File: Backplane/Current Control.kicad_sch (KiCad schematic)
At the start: 28 parts, among them Q25 TPHR8504PL,LQ(M1W, Q26 TPHR8504PL,LQ(M1W, U28 LM393, U29 UCC27324DR, U3 LM358, U32 MCP4725A0T-E/CH, U33 MCP4725A0T-E/CH

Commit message: Done with layout for first current control
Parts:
- U3: footprint (none) -> COMPONENTS:SOP-8_L4.9-W3.9-P1.27-LS6.0-BL

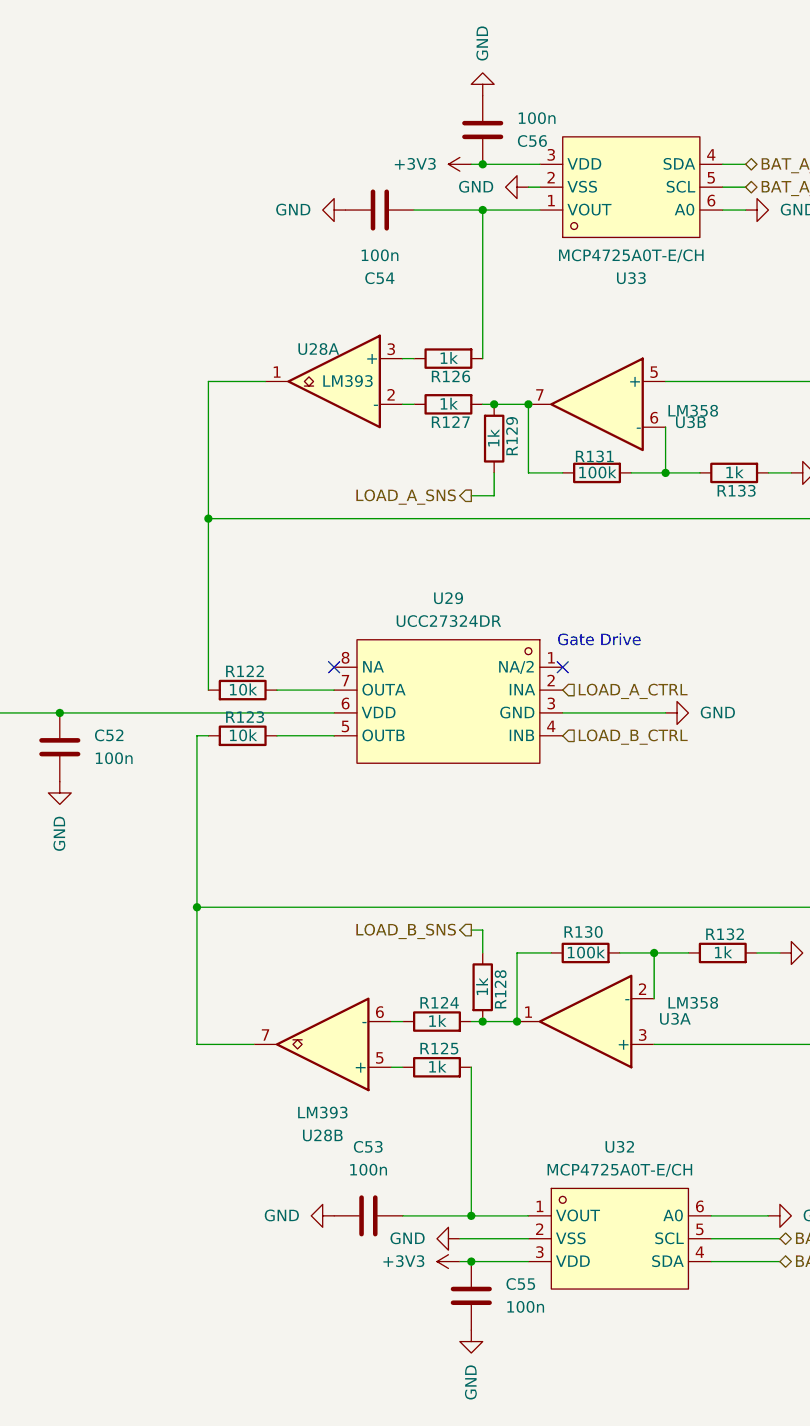
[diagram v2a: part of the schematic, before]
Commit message: First draft routing done.
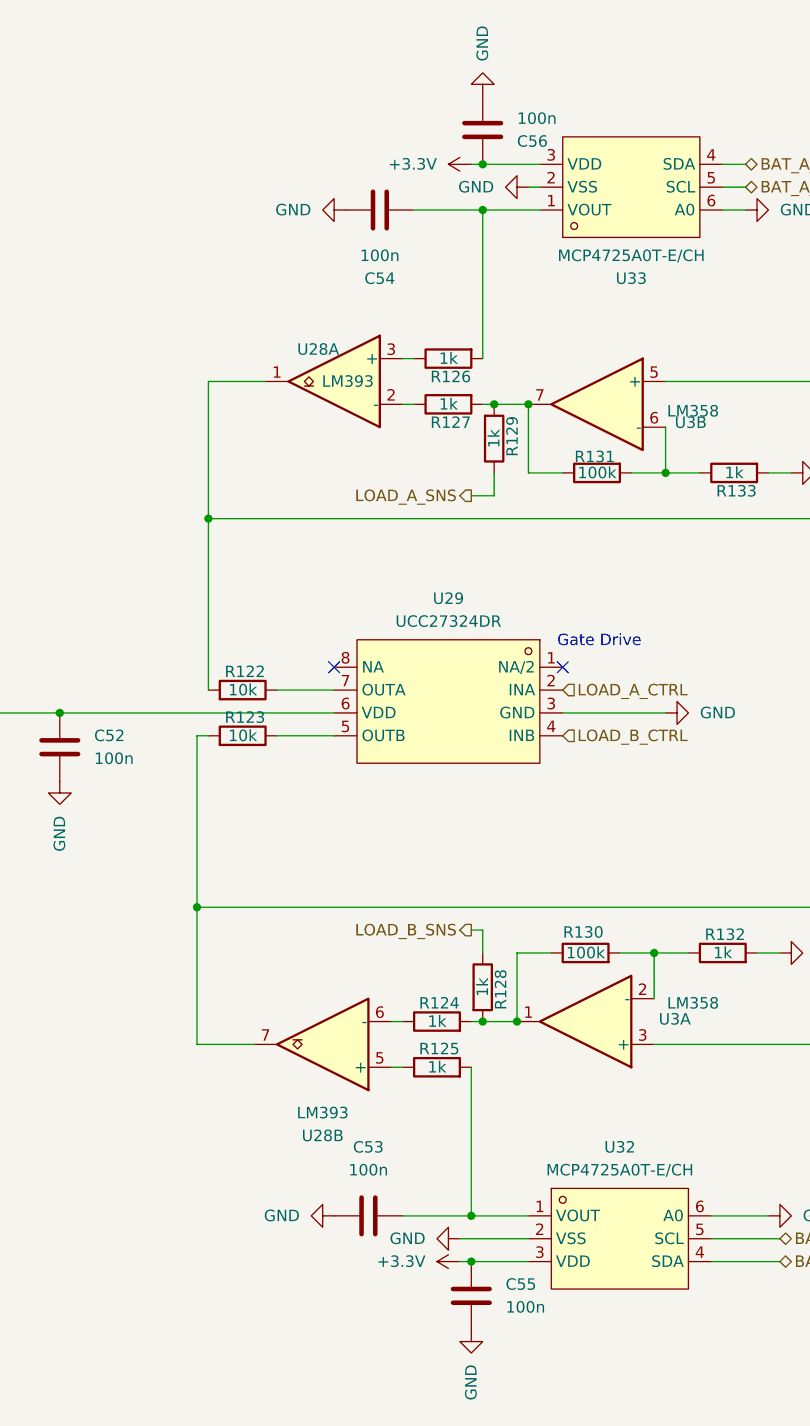
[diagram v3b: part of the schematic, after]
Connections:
- net +3V3 renamed +3.3V
